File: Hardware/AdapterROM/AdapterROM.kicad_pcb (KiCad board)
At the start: 2 copper layers, 30.1 x 38.1 mm, 2 parts, among them J1 ROM, U1 28C256

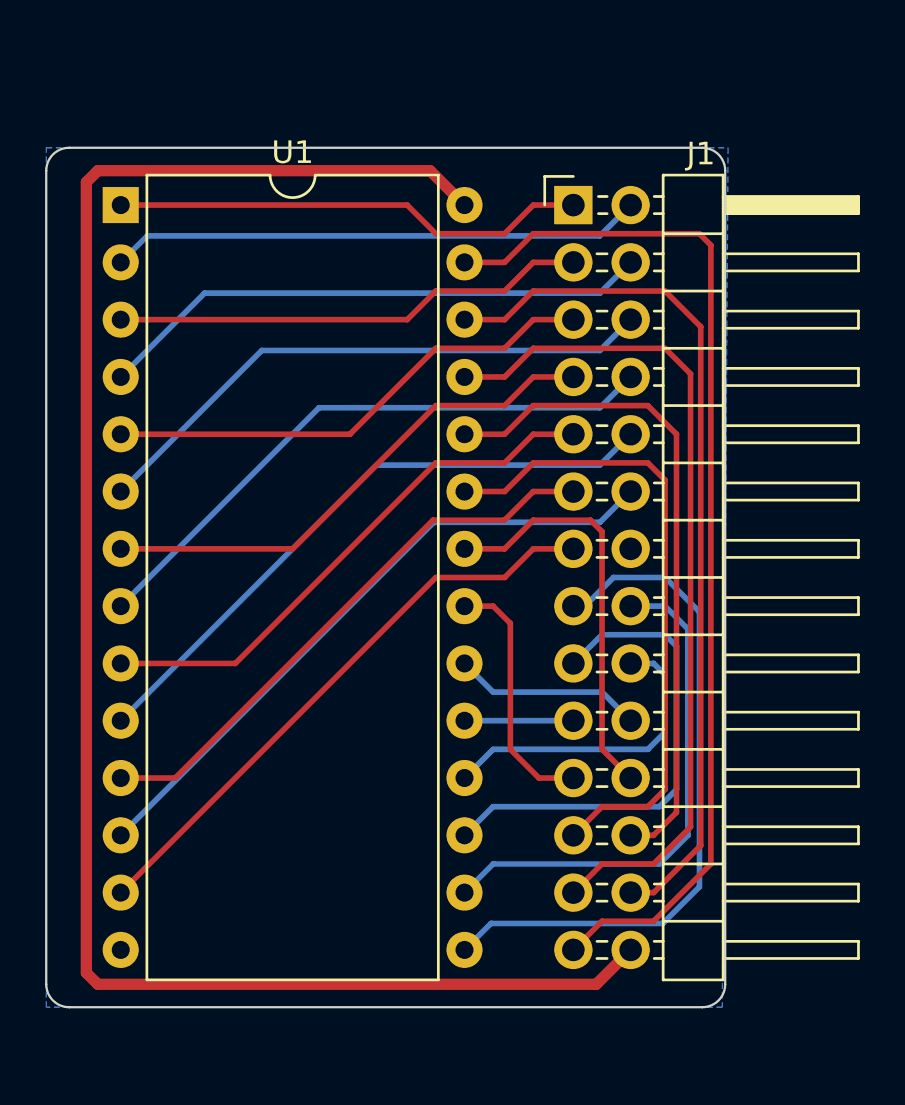
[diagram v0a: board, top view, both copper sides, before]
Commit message: implement graphic loading from ROM
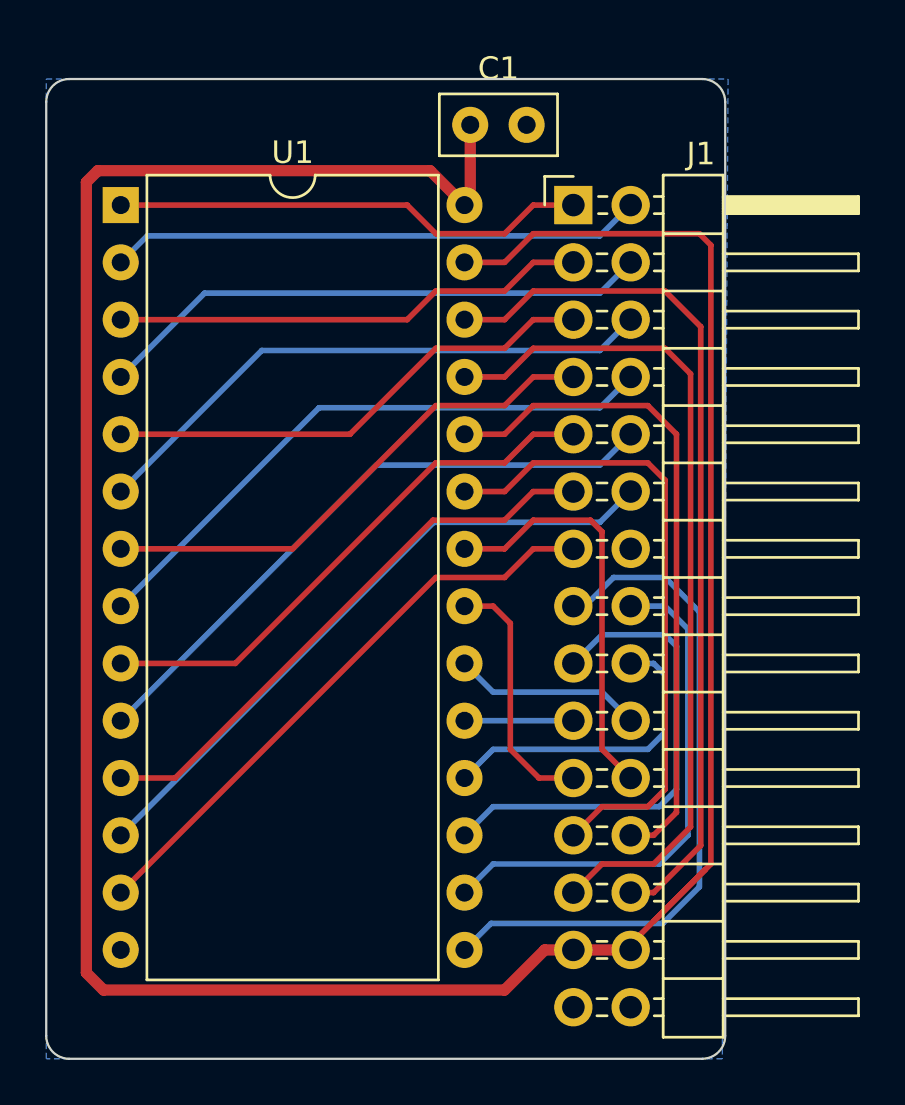
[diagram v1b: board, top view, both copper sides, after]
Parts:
- added C1: 100nF, Capacitor_THT:C_Disc_D5.0mm_W2.5mm_P2.50mm, F.Cu at (117.3, 47.5)
- J1: footprint Connector_PinHeader_2.54mm:PinHeader_2x14_P2.54mm_Horizontal -> Connector_PinHeader_2.54mm:PinHeader_2x15_P2.54mm_Horizontal
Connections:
- J1 pad 27: WE -> +5V
- U1 pad 27: WE -> +5V
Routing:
- net +5V: track 77.6 -> 129.1 mm
- net WE: track 46.8 -> 0.00 mm
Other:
- board size 30.1 x 38.1 mm -> 30.1 x 43.4 mm
